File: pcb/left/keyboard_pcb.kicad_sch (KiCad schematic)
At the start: 33 parts, among them J1 TRRS, K00 KEYSW, K01 KEYSW, K02 KEYSW, K03 KEYSW, K04 KEYSW, K05 KEYSW, K10 KEYSW, K11 KEYSW, K12 KEYSW, K13 KEYSW, K14 KEYSW, K15 KEYSW, K20 KEYSW, K21 KEYSW, K22 KEYSW, K23 KEYSW, K24 KEYSW, K25 KEYSW, K30 KEYSW, K31 KEYSW, K32 KEYSW, U2 Pico

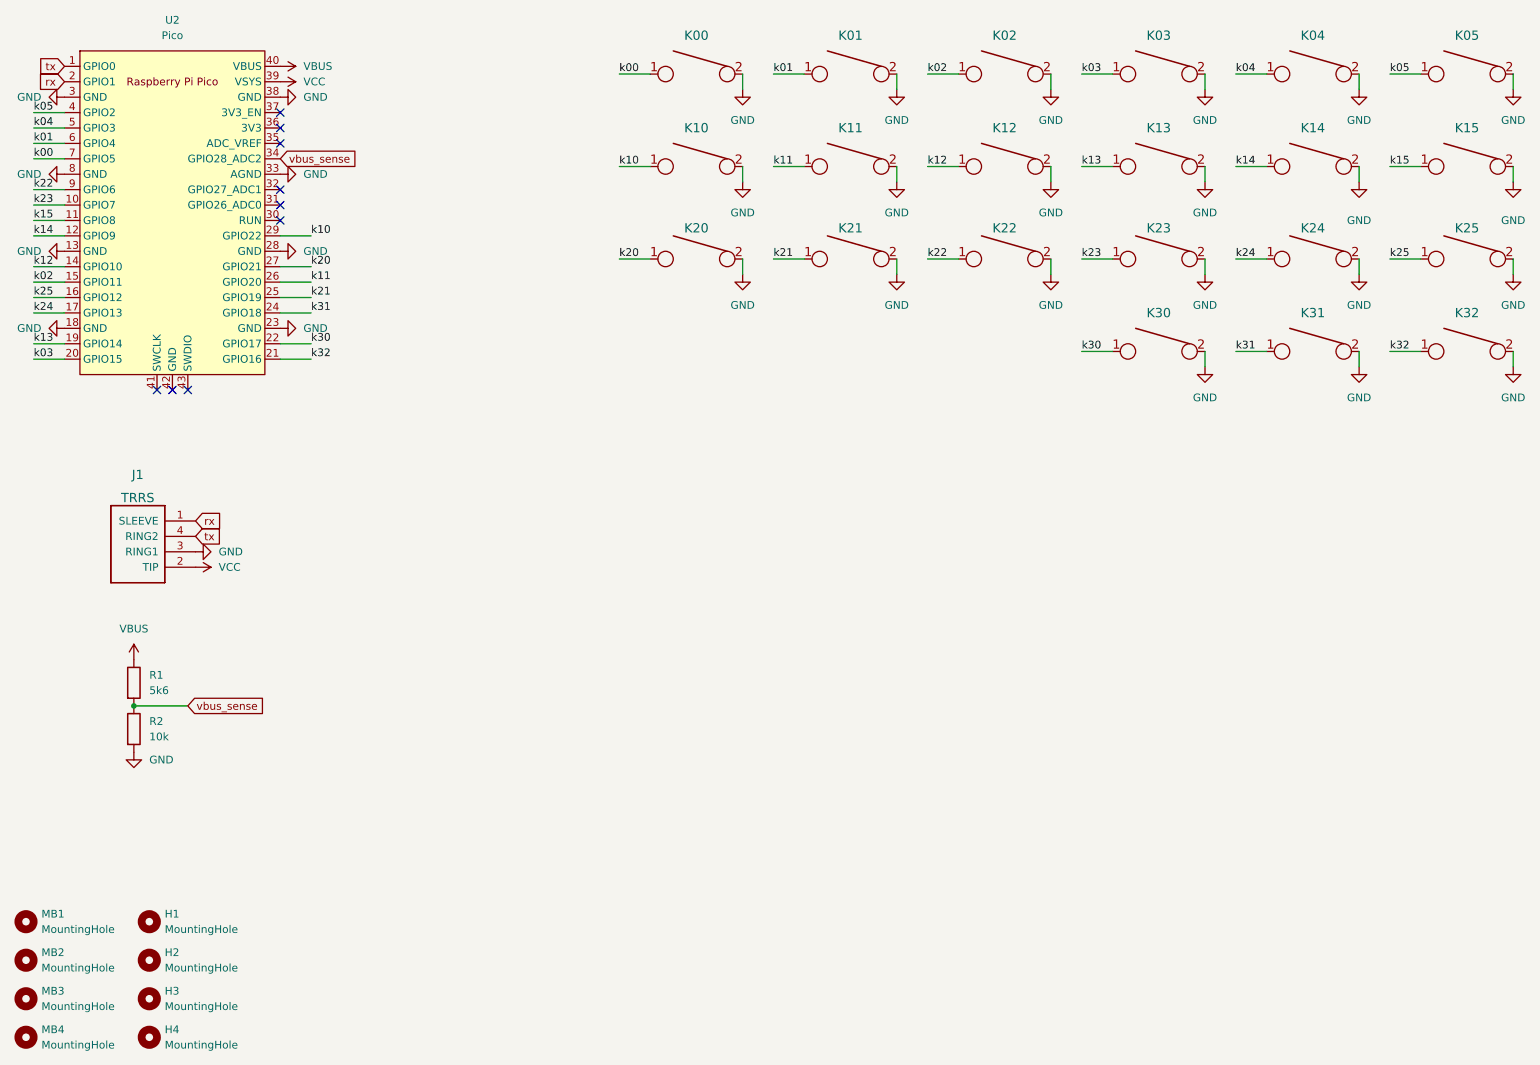
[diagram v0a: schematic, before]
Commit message: Added GPIO portexpander, Pin remapping, added LEDs WIP!
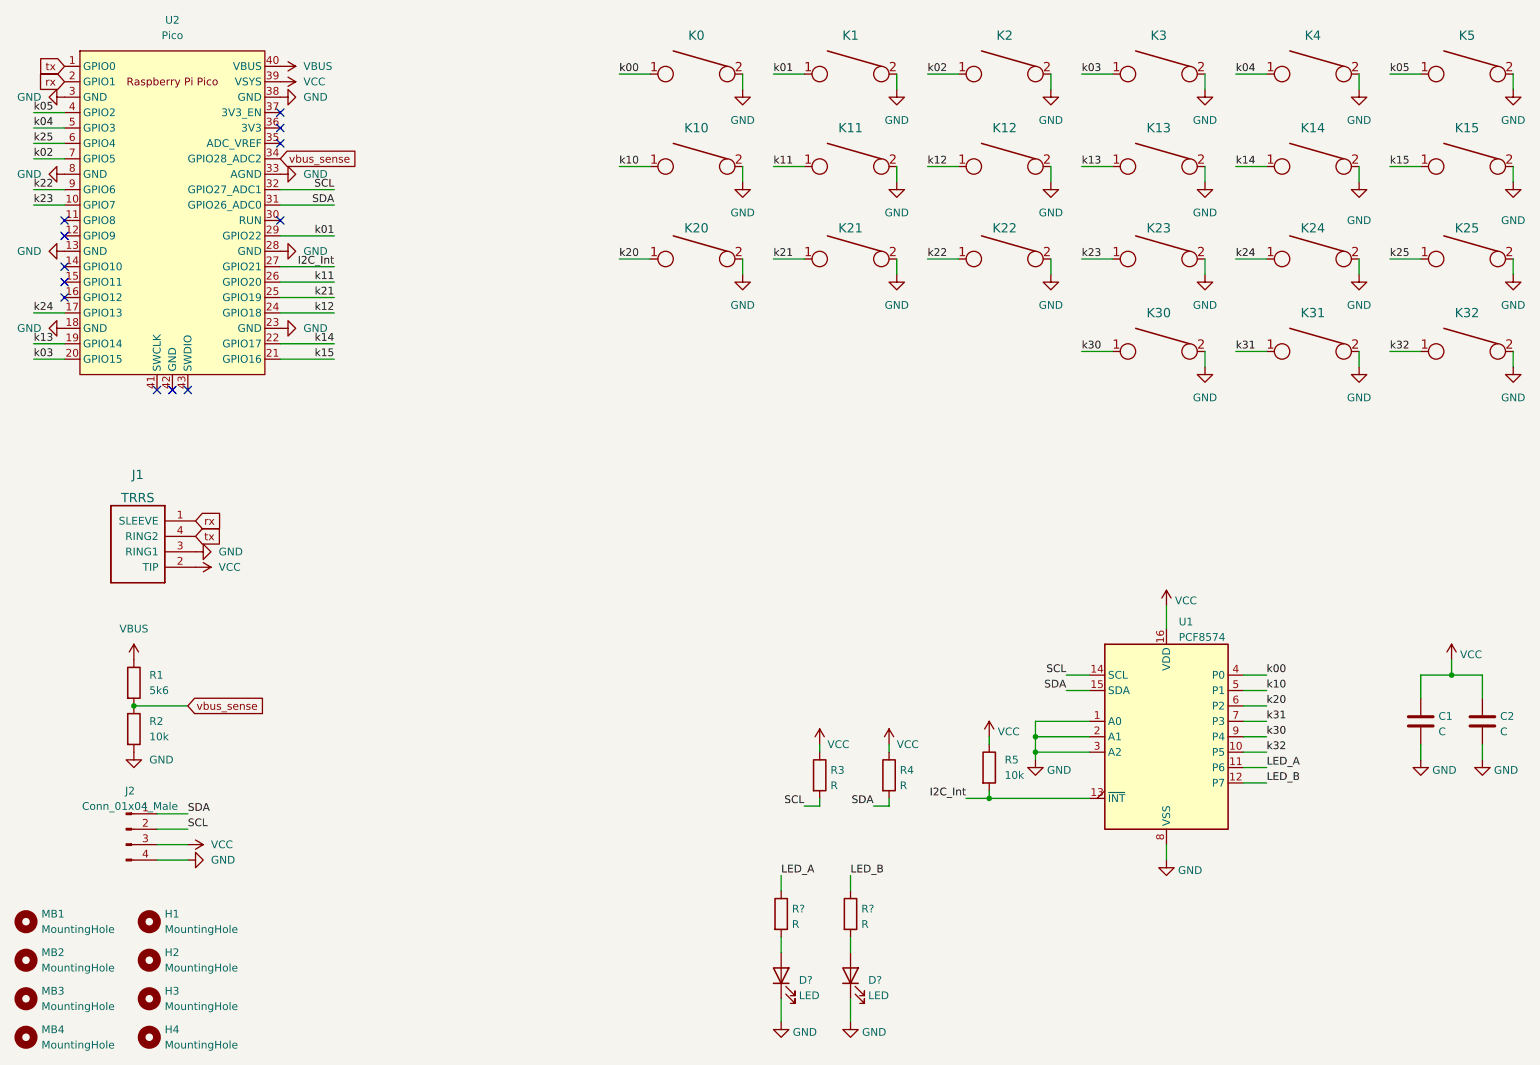
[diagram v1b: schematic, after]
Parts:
- added C1, C2: C, Capacitor_SMD:C_0603_1608Metric_Pad1.08x0.95mm_HandSolder, symbol Device:C
- added D? (x2): LED, symbol Device:LED
- added J2: Conn_01x04_Male, Connector_PinHeader_2.54mm:PinHeader_1x04_P2.54mm_Vertical, symbol Connector:Conn_01x04_Male
- added R3, R4, R? (x2): R, Resistor_SMD:R_0603_1608Metric_Pad0.98x0.95mm_HandSolder, symbol Device:R
- added R5: 10k, Resistor_SMD:R_0603_1608Metric_Pad0.98x0.95mm_HandSolder, symbol Device:R
- added U1: PCF8574, Package_SO:SSOP-20_4.4x6.5mm_P0.65mm, symbol Interface_Expansion:PCF8574
- J1: footprint Resistor_SMD:R_1206_3216Metric_Pad1.30x1.75mm_HandSolder -> trrs_audiojack:TRRS-PJ-320A
- R1, R2: footprint Resistor_SMD:R_1206_3216Metric_Pad1.30x1.75mm_HandSolder -> Resistor_SMD:R_0603_1608Metric_Pad0.98x0.95mm_HandSolder
- renumbered K00 to K0, K01 to K1, K02 to K2, K03 to K3, K04 to K4, K05 to K5
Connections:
- net GND: now also C1.2, C2.2, D?.1 (K), D?.1 (K), J2.4 (Pin_4), U1.1 (A0), U1.2 (A1), U1.3 (A2), U1.8 (VSS)
- net VCC: now also C1.1, C2.1, J2.3 (Pin_3), R3.1, R4.1, R5.1, U1.16 (VDD)
- net k00: now also U1.4 (P0); no longer U2.7 (GPIO5)
- net k01: now also U2.29 (GPIO22); no longer U2.6 (GPIO4)
- net k02: now also U2.7 (GPIO5); no longer U2.15 (GPIO11)
- net k10: now also U1.5 (P1); no longer U2.29 (GPIO22)
- net k12: now also U2.24 (GPIO18); no longer U2.14 (GPIO10)
- net k14: now also U2.22 (GPIO17); no longer U2.12 (GPIO9)
- net k15: now also U2.21 (GPIO16); no longer U2.11 (GPIO8)
- net k20: now also U1.6 (P2); no longer U2.27 (GPIO21)
- net k25: now also U2.6 (GPIO4); no longer U2.16 (GPIO12)
- net k30: now also U1.9 (P4); no longer U2.22 (GPIO17)
- net k31: now also U1.7 (P3); no longer U2.24 (GPIO18)
- net k32: now also U1.10 (P5); no longer U2.21 (GPIO16)
- net SDA: now reaches U2.31 (GPIO26_ADC0)
- net SDA: now also J2.1 (Pin_1), R4.2, U1.15 (SDA)
- net SCL: now reaches U2.32 (GPIO27_ADC1)
- net SCL: now also J2.2 (Pin_2), R3.2, U1.14 (SCL)
- new net: D?.2 (A), R?.2 (x2)
- new net I2C_Int: R5.2, U1.13 (~{INT}), U2.27 (GPIO21)
- new net LED_A: R?.1, U1.11 (P6)
- new net LED_B: R?.1, U1.12 (P7)
- no-connect marks 9 -> 12
